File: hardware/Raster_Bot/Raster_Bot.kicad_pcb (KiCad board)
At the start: 2 copper layers, 62 x 33.6 mm, 68 parts, among them J1 JST_PH, J2 USB_C_Receptacle_USB2.0_16P, J3 Conn_Motor_N20_Encoder, J4 Conn_EYESPI, J5 JUMPER_2PIN, J6 Conn_Motor_N20_Encoder, J8 JUMPER_2PIN, Q1 AO3401A, SW1 SW_SPDT_SH, SW2 SW_RESET, SW3 SW_BOOT, U1 BQ24072RGT, U2 ESP32-S3-WROOM-1, U3 DRV8833PWPR, U4 AP2114H-3.3, U5 TPS61023DRLR

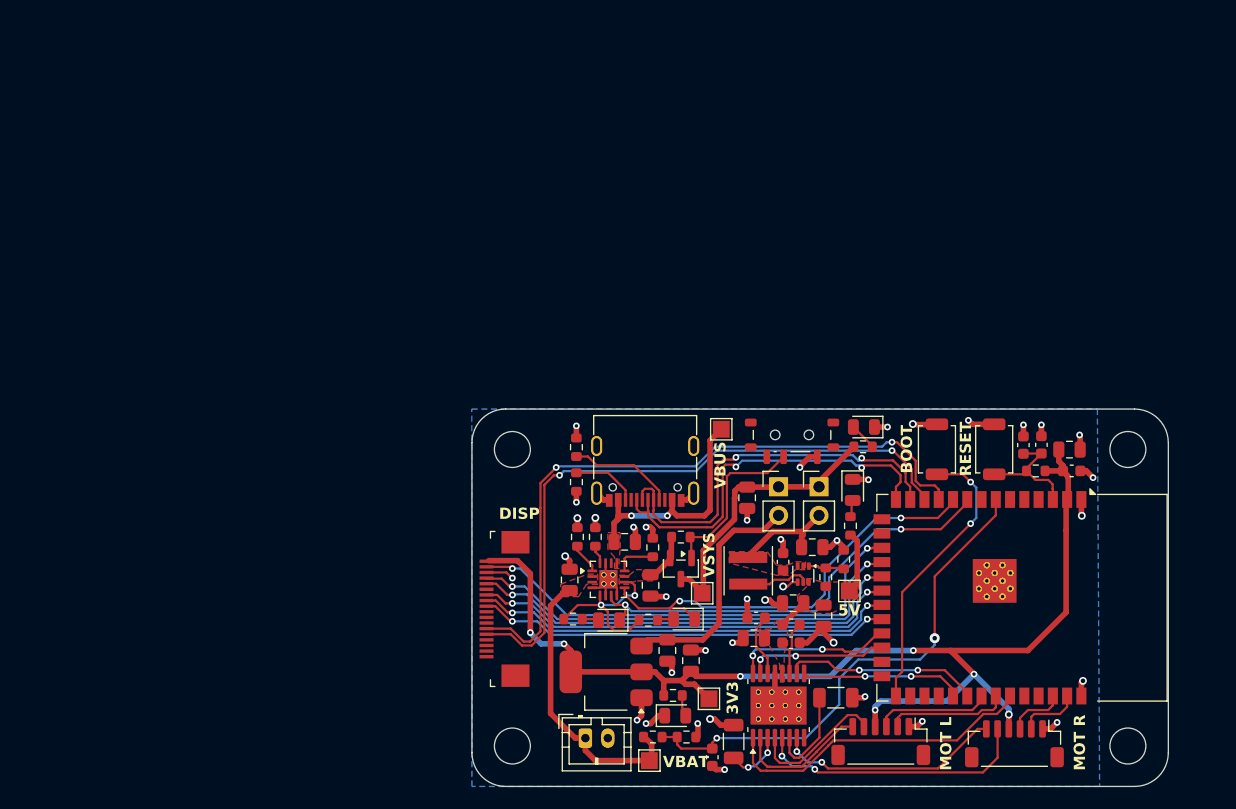
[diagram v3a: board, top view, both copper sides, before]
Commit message: [hardware] v0.4 - 4 layer PCB design with ESP32-S3-MINI
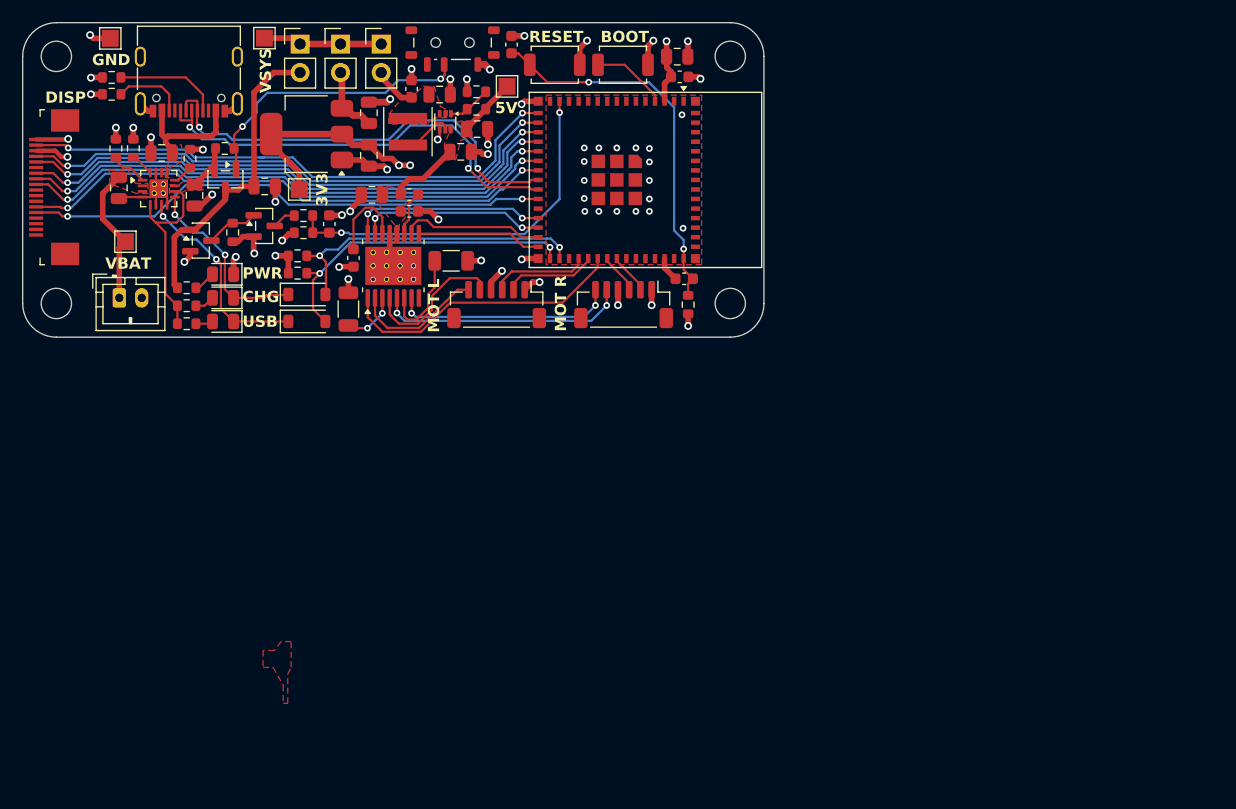
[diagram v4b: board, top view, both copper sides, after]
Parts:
- removed the C14 at (131.4, 108.8)
- removed the C19 at (134.5, 85.7)
- removed the C4 at (160.7, 81.0)
- removed the C5 at (163.4, 83.3)
- removed the R16 at (128.6, 89.2)
- removed the R8 at (160.2, 83.3)
- removed TP2: TestPoint, TestPoint:TestPoint_Pad_1.5x1.5mm
- removed the U2 at (159.0, 94.6)
- added C10: 0.1uF, Capacitor_SMD:C_0603_1608Metric, F.Cu at (128.5, 48.2)
- added C12: 22uF, Capacitor_SMD:C_0805_2012Metric, F.Cu at (128.3, 46.4)
- added C7: 1uF, Capacitor_SMD:C_0603_1608Metric, F.Cu at (128.9, 66.2)
- added C9: 0.1uF, Capacitor_SMD:C_0603_1608Metric, F.Cu at (97.3, 61.3)
- added J8: JUMPER_2PIN, Connector_PinHeader_2.54mm:PinHeader_1x02_P2.54mm_Vertical, F.Cu at (94.7, 45.3)
- added Q2: AO3401A, Package_TO_SOT_SMD:SOT-23, F.Cu at (91.5, 61.5)
- added Q3: 2N7002, Package_TO_SOT_SMD:SOT-23, F.Cu at (85.9, 62.8)
- added R12: 10k, Resistor_SMD:R_0603_1608Metric, F.Cu at (129.2, 68.5)
- added R13: 100k, Resistor_SMD:R_0603_1608Metric, F.Cu at (88.7, 62.1)
- added R9: 10k, Resistor_SMD:R_0603_1608Metric, F.Cu at (94.5, 65.7)
- added TP6: TestPoint, TestPoint:TestPoint_Pad_1.5x1.5mm, F.Cu at (77.8, 44.8)
- added U3: ESP32-S3-MINI-1, Raster_Bot:ESP32-S3-MINI-1, F.Cu at (125.5, 57.4)
- D4, D5: value LED -> SD103AW; footprint LED_SMD:LED_0805_2012Metric -> Diode_SMD:D_SOD-123
- H1, H2, H3, H4: footprint MountingHole:MountingHole_3.2mm_M3 -> MountingHole:MountingHole_2.7mm_M2.5
- R10: value 2.2k -> 10k
- R11: value 2.2k -> 100k
- R14, R15: value 200k -> 100k
- R3: renamed from R9; value 2.2k -> 4.7k
- R6, R7: value 2.2k -> 4.7k
- moved C6 75.4 mm to (91.5, 58.0)
- moved R11 63.0 mm to (88.0, 54.6)
- moved TP3 62.9 mm to (91.5, 44.8)
- moved R3 61.9 mm to (84.6, 67.0)
- moved D1 58.7 mm to (87.8, 65.8)
- moved TP4 58.2 mm to (94.6, 58.2)
- moved C13 57.9 mm to (113.5, 45.4)
- moved J1 57.1 mm to (78.6, 67.9)
- moved H2 56.6 mm to (73.0, 68.4)
- moved R15 56.4 mm to (95.0, 62.1), turned to 180 degrees
- moved R14 55.9 mm to (95.0, 60.6)
- moved TP1 55.6 mm to (79.2, 62.9)
- moved J5 55.5 mm to (98.3, 45.3)
- moved J7 55.4 mm to (101.9, 45.3)
- moved J3 54.9 mm to (72.5, 58.0)
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- renumbered C12 to C1, C18 to C11, C7 to C13, C15 to C14, C16 to C15, C8 to C16, C9 to C17, C10 to C18, C11 to C19, C1 to C2, C13 to C3, C2 to C4, C3 to C5, C17 to C8, D3 to D1, D1 to D2, D2 to D3, J4 to J3, J3 to J4, J8 to J7, R17 to R16, R18 to R17, R12 to R18, R13 to R19, R3 to R4, R4 to R5, R5 to R8, U4 to U1, U1 to U2, U5 to U4, U3 to U5
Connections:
- net /VBAT_DIV renamed /VBAT_MON
- C6 pad 1: +3V3 -> /VSYS_SW
- D4 pad 1: GND -> /PGOOD
- D4 pad 2: Net-(D4-A) -> /PGOOD_MON
- D5 pad 1: GND -> /CHG
- D5 pad 2: Net-(D5-A) -> /CHG_MON
- Q1 pad 3: VSYS -> /VSYS_SW
- R10 pad 1: +5V -> +3V3
- R10 pad 2: Net-(D4-A) -> /CHG_MON
- R11 pad 1: +3V3 -> VSYS_SRC
- R11 pad 2: Net-(D5-A) -> Net-(Q1-G)
- R14 pad 1: VBAT -> Net-(Q2-D)
- R3 pad 1: VSYS -> /VSYS_SW
- TP1 pad 1: VBUS -> VBAT
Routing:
- net +3V3: track 105.1 -> 35.3 mm, vias 7 -> 8
- net /PGOOD_MON: track 0.00 -> 29.0 mm, vias 0 -> 2
- net /CHG_MON: track 0.00 -> 28.2 mm, vias 0 -> 2
- net /VSYS_SW: track 0.00 -> 27.3 mm
- net /RESET: track 10.9 -> 34.1 mm, vias 0 -> 2
- net /CHG: track 38.9 -> 16.6 mm
- net /PGOOD: track 39.5 -> 18.5 mm
- net /BOOT: track 25.5 -> 6.74 mm, vias 2 -> 0
- net /VSYS_3VIN: track 21.1 -> 6.20 mm
- net VSYS: track 25.2 -> 10.6 mm
- net /VBAT_MON: track 45.9 -> 33.5 mm
- net /CS: track 37.2 -> 48.8 mm
- net /RST: track 37.7 -> 49.1 mm
- net /SCL: track 59.5 -> 48.1 mm
- net /DC: track 38.6 -> 49.2 mm
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- added copper zone on In2.Cu, net +3V3
- added copper zone on F.Cu, net GND
- added copper zone on In1.Cu, net GND
- removed copper zone on B.Cu, net GND
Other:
- board size 62 x 33.6 mm -> 66 x 28 mm
- copper layers 2 -> 4
- board text added: "CHG"
- board text added: "GND"
- board text added: "PWR"
- board text added: "USB"
- board text removed: "VBUS"

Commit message: [hardware] v0.5 - Add motor driver bulk capacitor; Remove test pads and jumpers
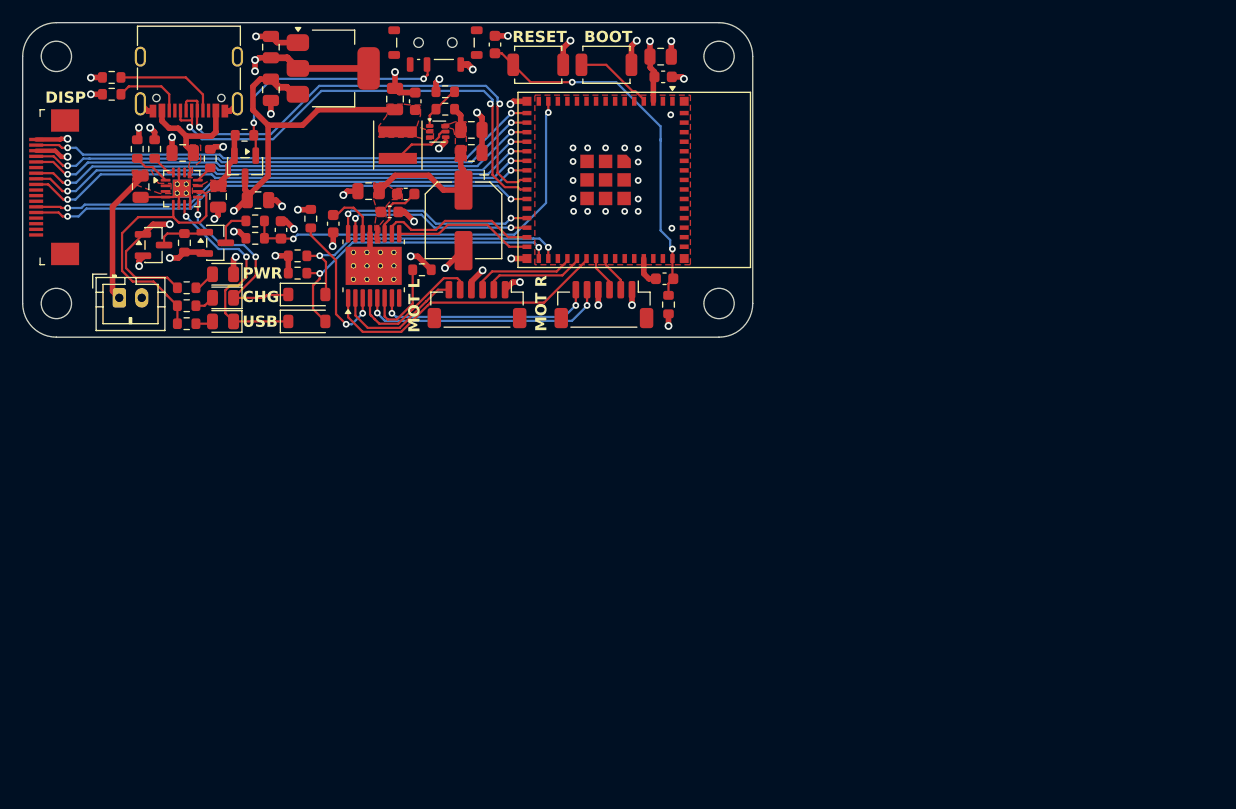
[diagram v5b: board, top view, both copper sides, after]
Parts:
- removed J5, J7, J8: JUMPER_2PIN, Connector_PinHeader_2.54mm:PinHeader_1x02_P2.54mm_Vertical
- removed TP1, TP3, TP4, TP5, TP6: TestPoint, TestPoint:TestPoint_Pad_1.5x1.5mm
- added C20: 470uF, Capacitor_SMD:CP_Elec_6.3x7.7, F.Cu at (109.2, 61.0)
- R18, R19: value 0.2 -> 200m; footprint Resistor_SMD:R_1206_3216Metric -> Resistor_SMD:R_0603_1608Metric
- moved C3 13.0 mm to (92.1, 45.6), turned to 90 degrees
- moved C1 8.96 mm to (92.1, 49.4), turned to -90 degrees
- moved R18 8.72 mm to (95.7, 60.9)
- moved U1 6.31 mm to (97.7, 47.5), turned to 0 degrees
- moved Q2 4.60 mm to (87.2, 63.0)
- moved R13 4.40 mm to (84.4, 63.0)
- moved C9 4.33 mm to (93.0, 61.9)
- moved R15 4.33 mm to (90.7, 62.6)
- moved R14 4.33 mm to (90.7, 61.0)
- moved Q3 4.23 mm to (81.7, 63.2)
- moved C11 4.00 mm to (103.2, 50.2), turned to 90 degrees
- moved C16 3.54 mm to (97.7, 61.3)
- moved R16 2.78 mm to (107.6, 51.1)
- moved R17 2.78 mm to (107.6, 49.5)
- moved R19 2.72 mm to (105.5, 65.4)
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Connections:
- C1 pad 1: /VSYS_3VIN -> VSYS
- C11 pad 1: /VSYS_5VIN -> VSYS
- C6 pad 1: /VSYS_SW -> VSYS
- C8 pad 1: /VSYS_5VIN -> VSYS
- L1 pad 1: /VSYS_5VIN -> VSYS
- Q1 pad 3: /VSYS_SW -> VSYS
- Q3 pad 1: /VSYS_SW -> VSYS
- R3 pad 1: /VSYS_SW -> VSYS
- U1 pad 3: /VSYS_3VIN -> VSYS
- U3 pad 29: /MOT2_IN1 -> /MOT2_IN2
- U3 pad 30: /MOT2_IN2 -> /MOT2_IN1
- U4 pad 2: /VSYS_5VIN -> VSYS
- U4 pad 3: /VSYS_5VIN -> VSYS
- U5 pad 10: /MOT2_IN1 -> /MOT2_IN2
- U5 pad 9: /MOT2_IN2 -> /MOT2_IN1
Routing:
- net VSYS: track 10.6 -> 50.6 mm, vias 0 -> 2
- net /VSYS_SW: track 27.3 -> 0.00 mm
- net VBAT: track 30.2 -> 21.4 mm
- net Net-(U5-AISEN): track 5.03 -> 13.1 mm
- net +3V3: track 35.3 -> 27.6 mm
- net VSYS_SRC: track 21.3 -> 28.5 mm
- net /VSYS_3VIN: track 6.20 -> 0.00 mm
- net /VSYS_5VIN: track 4.04 -> 0.00 mm
- net /USB_D-: track 39.4 -> 43.2 mm
- net /LITE: track 49.7 -> 46.0 mm
- net /USB_D+: track 39.7 -> 43.4 mm
- net /VBAT_MON: track 33.5 -> 37.0 mm
- net Net-(Q1-G): track 25.4 -> 22.0 mm
- net /RST: track 49.1 -> 45.9 mm
- net /MOSI: track 49.4 -> 46.2 mm
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- added copper zone on F.Cu, net VSYS
- removed copper zone on F.Cu, net /VSYS_5VIN
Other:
- board size 66 x 28 mm -> 65 x 28 mm
- board text removed: "3V3"
- board text removed: "5V"
- board text removed: "GND"
- board text removed: "VBAT"
- board text removed: "VSYS"

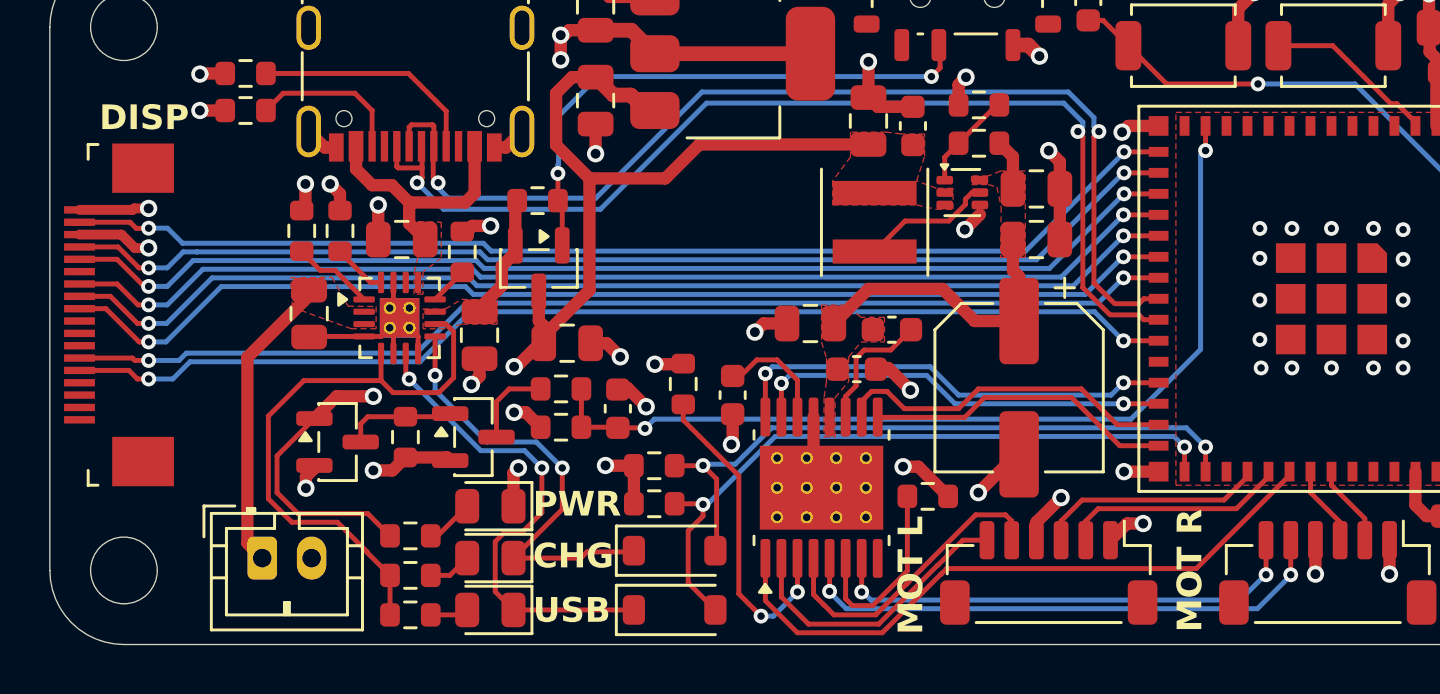
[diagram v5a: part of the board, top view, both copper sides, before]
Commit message: [hardware] Chage ISEN resistor values, part, and placement
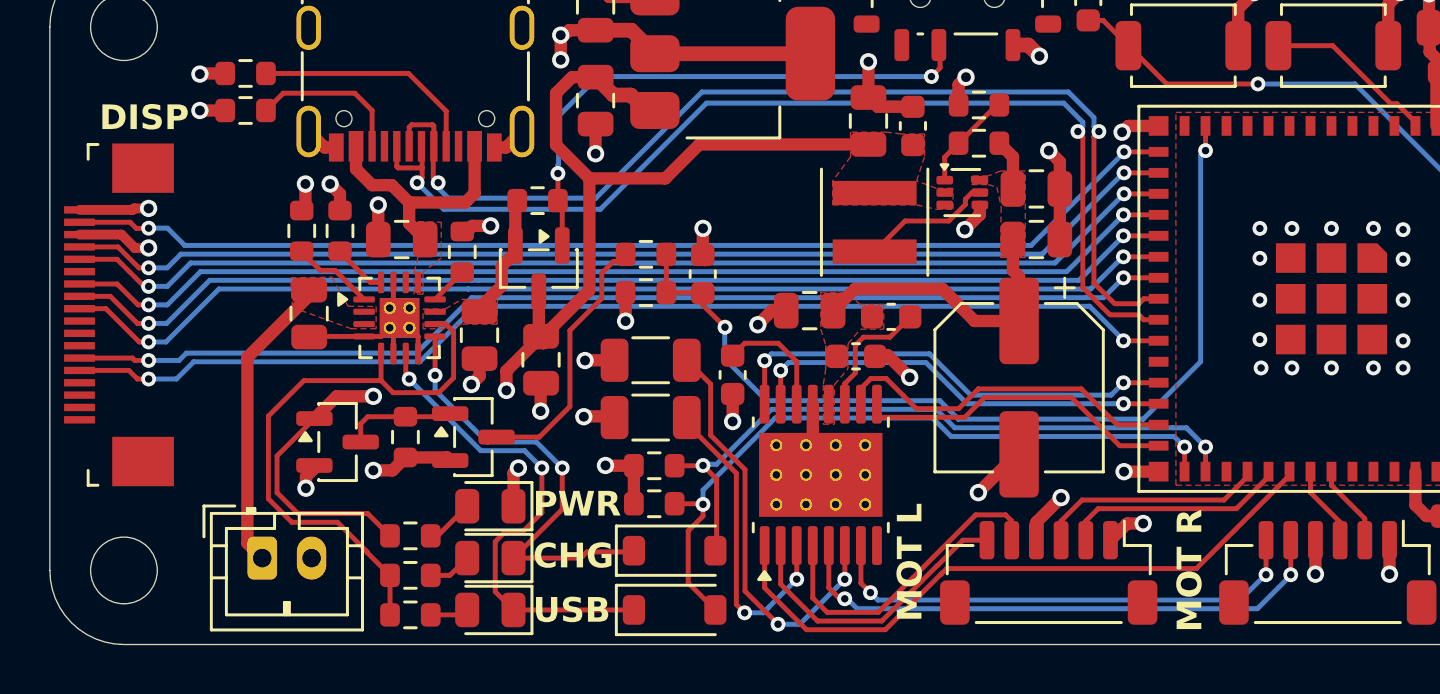
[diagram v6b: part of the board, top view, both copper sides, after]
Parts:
- R18, R19: value 200m -> 300m; footprint Resistor_SMD:R_0603_1608Metric -> Resistor_SMD:R_1206_3216Metric
- moved R19 12.5 mm to (94.3, 59.9), turned to 180 degrees
- moved C9 6.44 mm to (96.4, 56.4)
- moved R15 6.44 mm to (94.1, 57.1)
- moved R14 6.44 mm to (94.1, 55.6)
- moved R18 1.90 mm to (94.3, 62.2), turned to 180 degrees
- moved C6 1.25 mm to (89.9, 59.9), turned to -90 degrees
- moved C16 0.82 mm to (97.7, 60.5)
- moved C18 0.52 mm to (102.6, 59.7)
- moved C17 0.52 mm to (104.1, 58.1)
- moved C19 0.52 mm to (100.8, 57.9)
- moved U5 0.52 mm to (101.2, 64.5)
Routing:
- net Net-(U5-BISEN): track 7.90 -> 17.2 mm, vias 0 -> 2
- net Net-(Q2-D): track 3.44 -> 10.6 mm
- net GND: track 76.3 -> 73.9 mm
- net /PGOOD_MON: track 28.0 -> 28.9 mm
- net /CHG_MON: track 27.1 -> 27.7 mm
- net /MOT1_M2: track 12.4 -> 12.9 mm

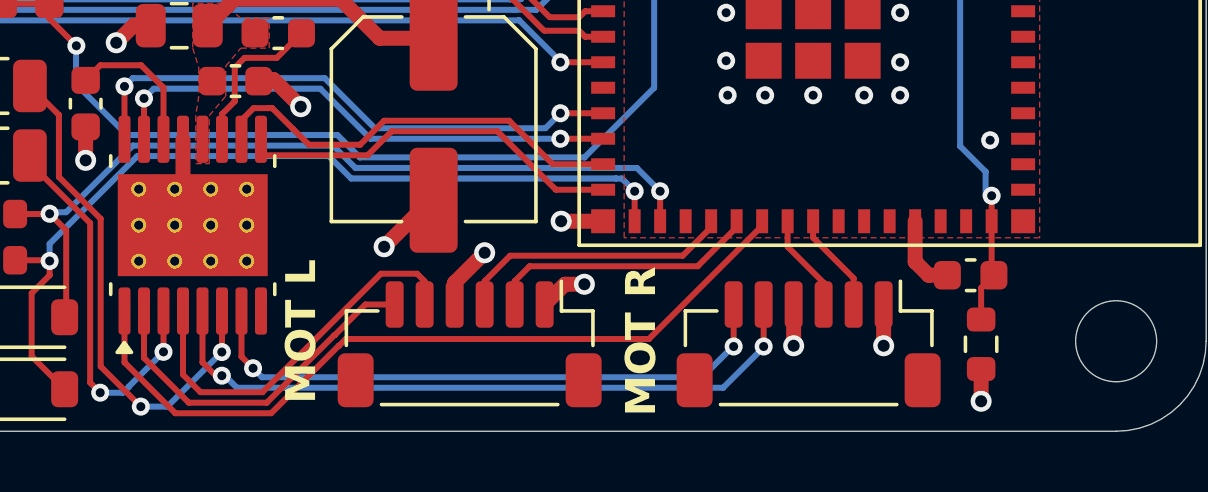
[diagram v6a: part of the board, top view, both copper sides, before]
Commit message: [hardware] v0.6 - Add silkscreen logo; Reposition footprints; Remove custom USB footprint
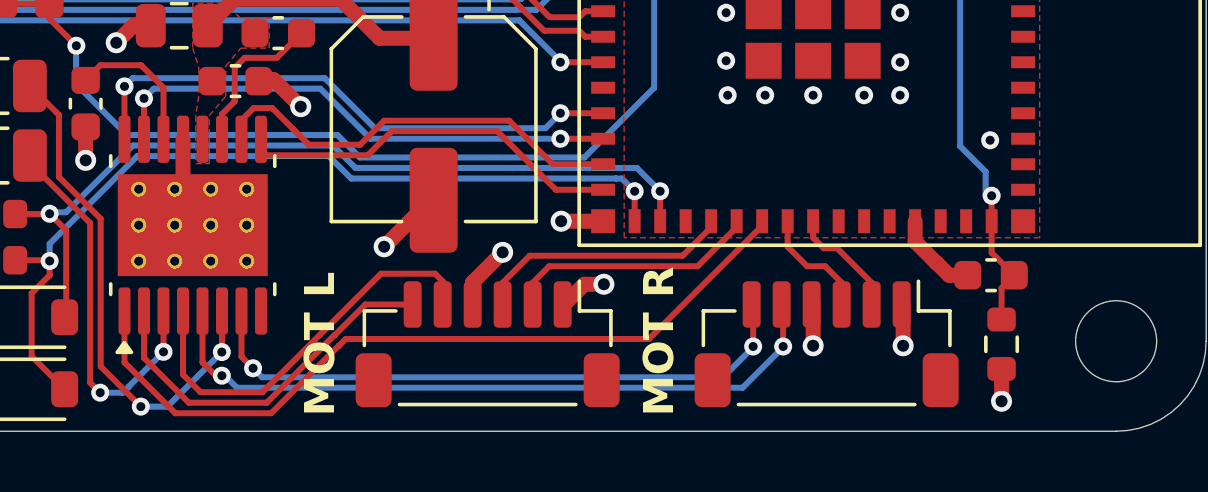
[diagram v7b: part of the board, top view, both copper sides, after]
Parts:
- added G***: LOGO, Raster_Bot:Raster_Logo, B.Cu at (116.4, 51.6)
- moved R12 0.68 mm to (128.2, 68.5)
- moved C7 0.68 mm to (127.8, 66.2)
- moved J4 0.60 mm to (111.0, 68.5)
- moved J6 0.60 mm to (122.3, 68.5)
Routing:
- net /MOT2_M1: track 20.1 -> 20.8 mm
- net /MOT2_M2: track 22.8 -> 23.4 mm
- net /MOT1_ENCB: track 9.12 -> 8.49 mm
- net /MOT1_ENCA: track 9.27 -> 8.64 mm
- net /MOT1_M2: track 12.9 -> 13.5 mm
- net /MOT1_M1: track 11.9 -> 12.5 mm
- net /MOT2_ENCA: track 3.52 -> 4.12 mm
- net /MOT2_ENCB: track 3.33 -> 3.85 mm
